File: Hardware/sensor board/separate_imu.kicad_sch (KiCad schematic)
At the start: 0 parts

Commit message: Modified sensor board and separate sheet for IMU
Added footprints to internal pressure sensor, made changes from 11/11
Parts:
- added C1: 470nF, symbol Device:C_Small
- added FB1: 600R@100MHz, 200mA, symbol Device:FerriteBead
- added IMU1: ~, symbol New_Library:MTi_1
- added J1: Conn_01x04_Pin, symbol Connector:Conn_01x04_Pin
- added R1, R2: 2.7k, symbol Device:R
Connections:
- new net: IMU1.23 (I2C_SDA), J1.4 (Pin_4), R1.1
- new net: IMU1.24 (I2C_SCL), J1.3 (Pin_3), R2.1
- new net: C1.2, FB1.2, IMU1.5 (VDDA)
- new net GND: C1.1, IMU1.13 (GND), IMU1.25 (GND), IMU1.4 (GND), IMU1.8 (GND), J1.2 (Pin_2)
- new net VDD: FB1.1, IMU1.7 (VDDIO), J1.1 (Pin_1), R1.2, R2.2

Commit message: Changed labeling of resistors
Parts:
- renumbered R1 to R2, R2 to R3
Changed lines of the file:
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@@
   (symbol (lib_id "Device:R") (at 165.1 99.06 180) (unit 1)
     (in_bom yes) (on_board yes) (dnp no) (fields_autoplaced)
-    (property "Reference" "R1" (at 167.64 97.79 0)
+    (property "Reference" "R2" (at 167.64 97.79 0)
       (effects (font (size 1.27 1.27)) (justify right))
     )
@@
       (project "separate_imu"
         (path "/8a24fe02-04cc-49de-bd83-d8cbd4825e35"
-          (reference "R1") (unit 1)
+          (reference "R2") (unit 1)
         )
       )
@@
   (symbol (lib_id "Device:R") (at 175.26 99.06 180) (unit 1)
     (in_bom yes) (on_board yes) (dnp no) (fields_autoplaced)
-    (property "Reference" "R2" (at 177.8 97.79 0)
+    (property "Reference" "R3" (at 177.8 97.79 0)
       (effects (font (size 1.27 1.27)) (justify right))
     )
@@
       (project "separate_imu"
         (path "/8a24fe02-04cc-49de-bd83-d8cbd4825e35"
-          (reference "R2") (unit 1)
+          (reference "R3") (unit 1)
         )
       )

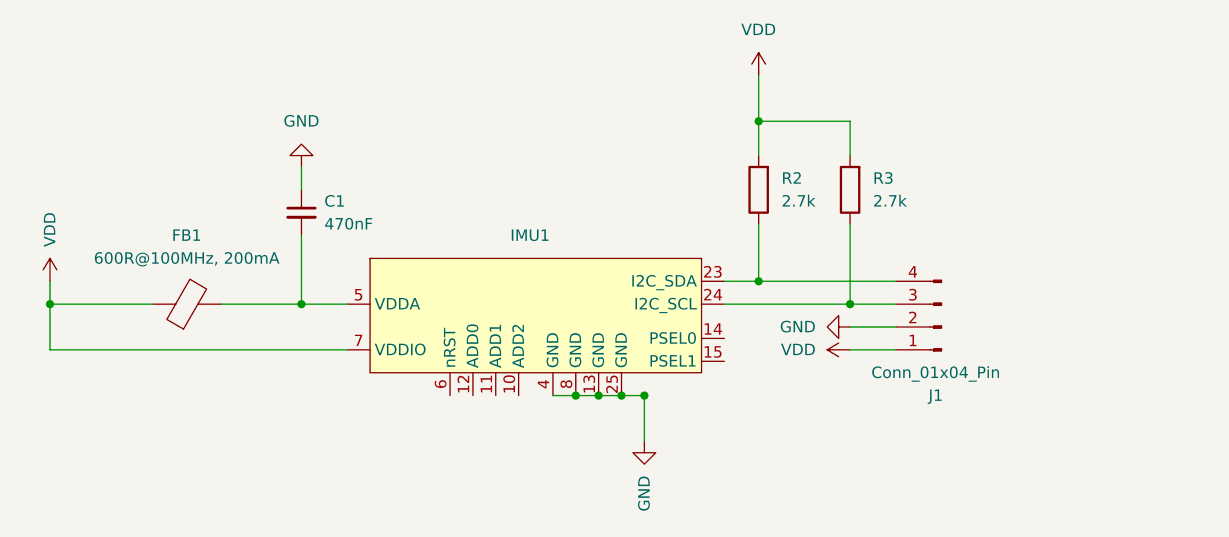
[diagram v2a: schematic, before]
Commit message: added imu sheet block + second connector into main sheet, minor symbol edits
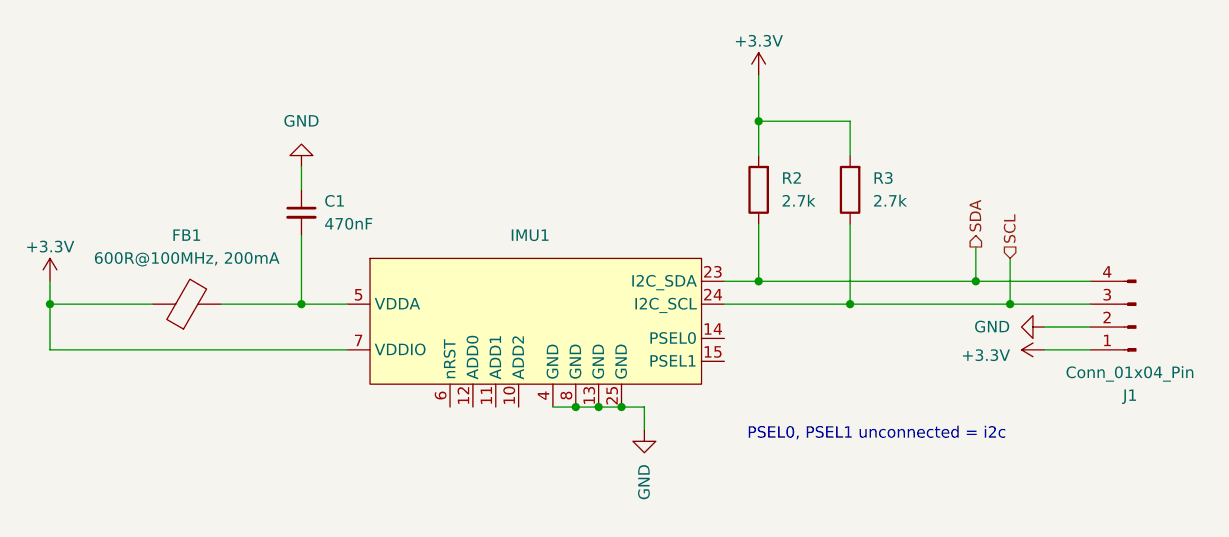
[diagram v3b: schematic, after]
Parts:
- IMU1: footprint (none) -> Package_LCC:PLCC-28_THT-Socket
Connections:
- net SDA: now reaches IMU1.23 (I2C_SDA), J1.4 (Pin_4), R2.1
- net SCL: now reaches IMU1.24 (I2C_SCL), J1.3 (Pin_3), R3.1
- net VDD renamed +3.3V
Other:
- note added: "PSEL0, PSEL1 unconnected = i2c"
- moved on the sheet: IMU1, J1

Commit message: changed symbol references
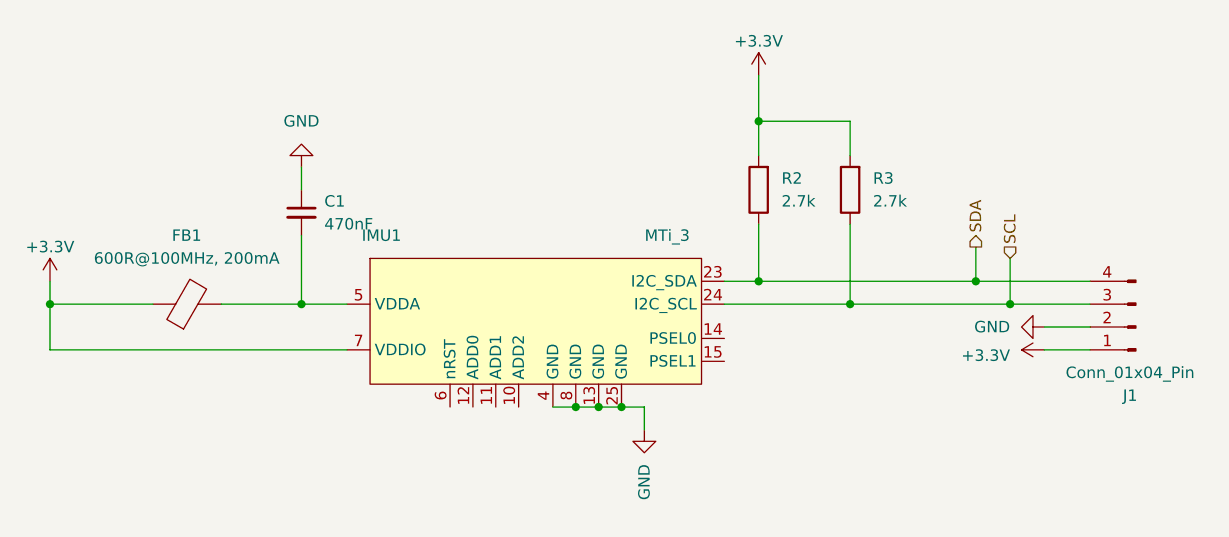
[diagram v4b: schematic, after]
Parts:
- IMU1: value ~ -> MTi_3; symbol New_Library:MTi_1 -> Sensor_Board_Components:MTi_3
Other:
- note removed: "PSEL0, PSEL1 unconnected = i2c"
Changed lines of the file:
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@@
     (stroke (width 0) (type default))
-  )
-  (text "PSEL0, PSEL1 unconnected = i2c" (at 163.83 127 0)
-    (effects (font (size 1.27 1.27)) (justify left bottom))
   )
   (hierarchical_label "SDA" (shape output) (at 189.23 105.41 90) (fields_autoplaced)
@@
     (effects (font (size 1.27 1.27)) (justify left))
   )
-  (symbol (lib_name "MTi_1_1") (lib_id "New_Library:MTi_1") (at 139.7 105.41 0) (unit 1)
+  (symbol (lib_id "Sensor_Board_Components:MTi_3") (at 139.7 105.41 0) (unit 1)
     (in_bom yes) (on_board yes) (dnp no)
-    (property "Reference" "IMU1" (at 139.7 104.14 0)
-      (effects (font (size 1.27 1.27)))
-    )
-    (property "Value" "~" (at 139.7 105.41 0)
+    (property "Reference" "IMU1" (at 123.19 104.14 0)
+      (effects (font (size 1.27 1.27)))
+    )
+    (property "Value" "MTi_3" (at 154.94 104.14 0)
       (effects (font (size 1.27 1.27)))
     )
@@
         )
         (path "/b809390c-5c7b-4faa-a505-ee668295313b/b45961e0-d21c-4cf1-a8fa-4e6b738a8420"
-          (reference "IMU1") (unit 1)
+          (reference "U1") (unit 1)
         )
       )
@@
         )
         (path "/b809390c-5c7b-4faa-a505-ee668295313b/b45961e0-d21c-4cf1-a8fa-4e6b738a8420"
-          (reference "#PWR015") (unit 1)
+          (reference "#PWR011") (unit 1)
         )
       )
@@
         )
         (path "/b809390c-5c7b-4faa-a505-ee668295313b/b45961e0-d21c-4cf1-a8fa-4e6b738a8420"
-          (reference "#PWR012") (unit 1)
+          (reference "#PWR09") (unit 1)
         )
       )
@@
         )
         (path "/b809390c-5c7b-4faa-a505-ee668295313b/b45961e0-d21c-4cf1-a8fa-4e6b738a8420"
-          (reference "#PWR010") (unit 1)
+          (reference "#PWR012") (unit 1)
         )
       )
@@
       (project "sensor board"
         (path "/b809390c-5c7b-4faa-a505-ee668295313b/b45961e0-d21c-4cf1-a8fa-4e6b738a8420"
-          (reference "R2") (unit 1)
+          (reference "R1") (unit 1)
         )
       )
@@
       (project "sensor board"
         (path "/b809390c-5c7b-4faa-a505-ee668295313b/b45961e0-d21c-4cf1-a8fa-4e6b738a8420"
-          (reference "#PWR011") (unit 1)
+          (reference "#PWR010") (unit 1)
         )
       )
@@
       (project "sensor board"
         (path "/b809390c-5c7b-4faa-a505-ee668295313b/b45961e0-d21c-4cf1-a8fa-4e6b738a8420"
-          (reference "R3") (unit 1)
+          (reference "R2") (unit 1)
         )
       )
@@
       (project "sensor board"
         (path "/b809390c-5c7b-4faa-a505-ee668295313b/b45961e0-d21c-4cf1-a8fa-4e6b738a8420"
-          (reference "J3") (unit 1)
-        )
-      )
+          (reference "J5") (unit 1)
+        )
+      )

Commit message: Added footprints to connectors
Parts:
- J1: footprint (none) -> Connector_JST:JST_XH_B4B-XH-AM_1x04_P2.50mm_Vertical
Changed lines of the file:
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@@
     (pin "1")
     (instances
+      (project "separate_imu"
+        (path "/8a24fe02-04cc-49de-bd83-d8cbd4825e35"
+          (reference "#PWR04") (unit 1)
+        )
+      )
       (project "sensor board"
         (path "/b809390c-5c7b-4faa-a505-ee668295313b"
@@
     (pin "1")
     (instances
+      (project "separate_imu"
+        (path "/8a24fe02-04cc-49de-bd83-d8cbd4825e35"
+          (reference "#PWR04") (unit 1)
+        )
+      )
       (project "sensor board"
         (path "/b809390c-5c7b-4faa-a505-ee668295313b"
@@
   )
   (symbol (lib_id "Connector:Conn_01x04_Pin") (at 207.01 114.3 180) (unit 1)
-    (in_bom yes) (on_board yes) (dnp no) (fields_autoplaced)
+    (in_bom yes) (on_board yes) (dnp no)
     (property "Reference" "J1" (at 206.375 121.92 0)
       (effects (font (size 1.27 1.27)))
@@
       (effects (font (size 1.27 1.27)))
     )
-    (property "Footprint" "" (at 207.01 114.3 0)
+    (property "Footprint" "Connector_JST:JST_XH_B4B-XH-AM_1x04_P2.50mm_Vertical" (at 207.01 114.3 0)
       (effects (font (size 1.27 1.27)) hide)
     )
@@
     (pin "1")
     (instances
+      (project "separate_imu"
+        (path "/8a24fe02-04cc-49de-bd83-d8cbd4825e35"
+          (reference "#PWR04") (unit 1)
+        )
+      )
       (project "sensor board"
         (path "/b809390c-5c7b-4faa-a505-ee668295313b"
@@
     )
   )
+  (sheet_instances
+    (path "/" (page "1"))
+  )
 )

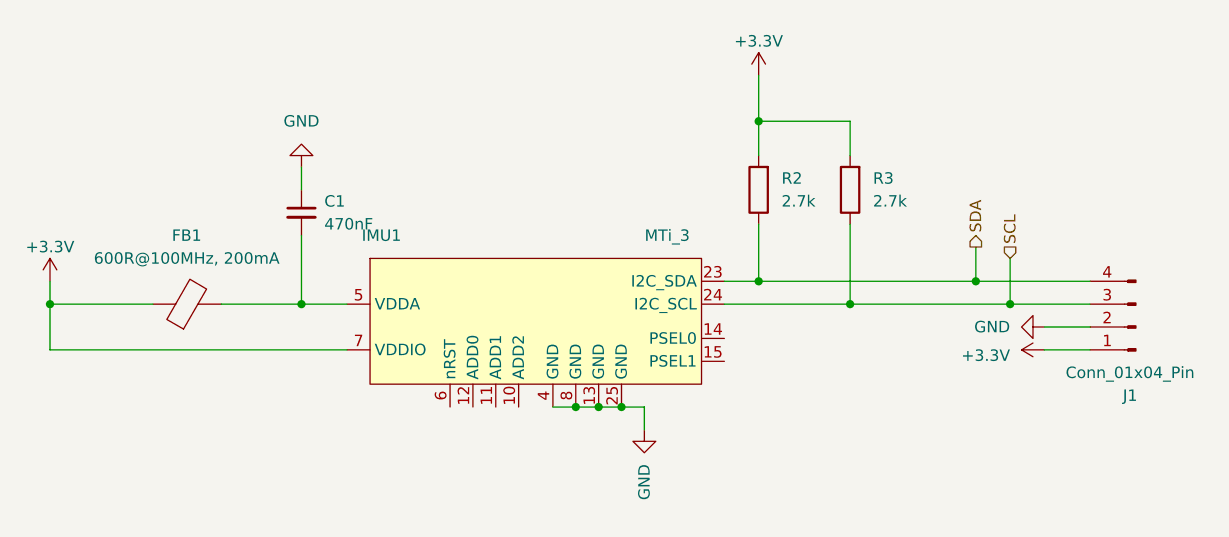
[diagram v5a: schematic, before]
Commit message: updated sensor board pcb with footprints
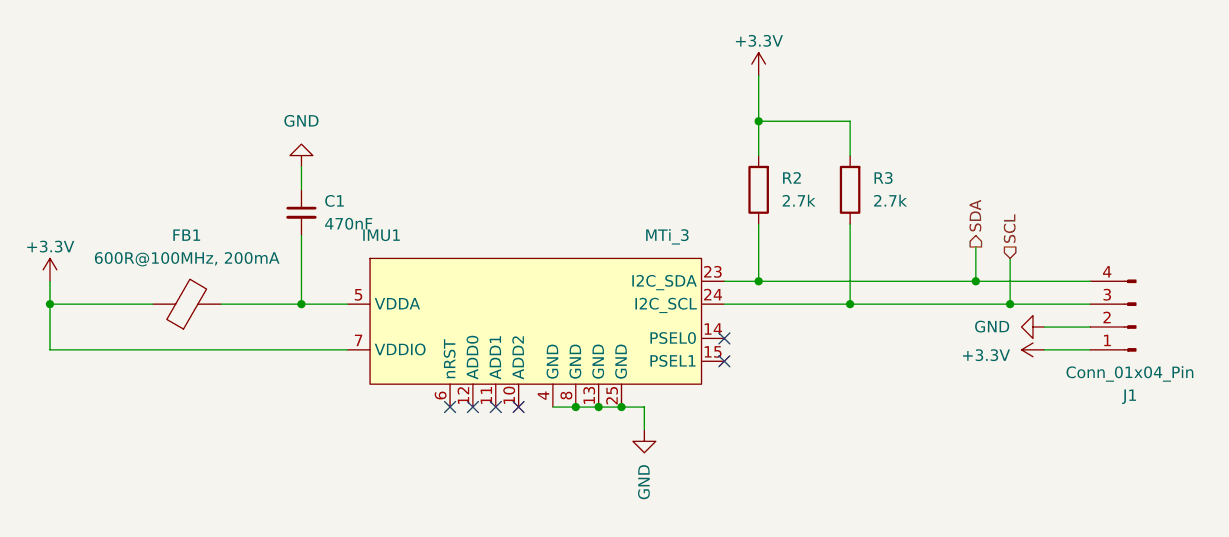
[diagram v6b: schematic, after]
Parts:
- C1: footprint (none) -> Capacitor_SMD:C_0805_2012Metric_Pad1.18x1.45mm_HandSolder
- FB1: footprint (none) -> Ferrite_SMD_AKL:Ferrite_0805_2012Metric_Pad1.15x1.40mm_BigPads
- R2, R3: footprint (none) -> Resistor_SMD:R_0805_2012Metric_Pad1.20x1.40mm_HandSolder
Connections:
- no-connect marks 0 -> 6
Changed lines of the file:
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@@
   (junction (at 165.1 91.44) (diameter 0) (color 0 0 0 0)
   )
+  (no_connect (at 130.81 123.19))
+  (no_connect (at 161.29 115.57))
+  (no_connect (at 138.43 123.19))
+  (no_connect (at 135.89 123.19))
+  (no_connect (at 133.35 123.19))
+  (no_connect (at 161.29 118.11))
   (wire (pts (xy 149.86 123.19) (xy 152.4 123.19))
     (stroke (width 0) (type default))
@@
       (effects (font (size 1.27 1.27)) (justify right))
     )
-    (property "Footprint" "" (at 166.878 99.06 90)
+    (property "Footprint" "Resistor_SMD:R_0805_2012Metric_Pad1.20x1.40mm_HandSolder" (at 166.878 99.06 90)
       (effects (font (size 1.27 1.27)) hide)
     )
@@
       (effects (font (size 1.27 1.27)))
     )
-    (property "Footprint" "" (at 101.6 113.538 90)
+    (property "Footprint" "Ferrite_SMD_AKL:Ferrite_0805_2012Metric_Pad1.15x1.40mm_BigPads" (at 101.6 113.538 90)
       (effects (font (size 1.27 1.27)) hide)
     )
@@
       (effects (font (size 1.27 1.27)) (justify left))
     )
-    (property "Footprint" "" (at 114.3 101.6 0)
+    (property "Footprint" "Capacitor_SMD:C_0805_2012Metric_Pad1.18x1.45mm_HandSolder" (at 114.3 101.6 0)
       (effects (font (size 1.27 1.27)) hide)
     )
@@
       (effects (font (size 1.27 1.27)) (justify right))
     )
-    (property "Footprint" "" (at 177.038 99.06 90)
-      (effects (font (size 1.27 1.27)) hide)
-    )
+    (property "Footprint" "Resistor_SMD:R_0805_2012Metric_Pad1.20x1.40mm_HandSolder" (at 177.038 99.06 90)
+      (effects (font (size 1.27 1.27)) hide)
+    )

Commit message: updated 3d models
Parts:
- J1: footprint Connector_JST:JST_XH_B4B-XH-AM_1x04_P2.50mm_Vertical -> Connector_JST:JST_XH_B4B-XH-A_1x04_P2.50mm_Vertical
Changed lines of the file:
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@@
       (effects (font (size 1.27 1.27)))
     )
-    (property "Footprint" "Connector_JST:JST_XH_B4B-XH-AM_1x04_P2.50mm_Vertical" (at 207.01 114.3 0)
+    (property "Footprint" "Connector_JST:JST_XH_B4B-XH-A_1x04_P2.50mm_Vertical" (at 207.01 114.3 0)
       (effects (font (size 1.27 1.27)) hide)
     )
